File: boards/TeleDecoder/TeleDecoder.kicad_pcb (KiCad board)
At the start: 2 copper layers, 39 x 49.5 mm, 62 parts, among them J1 USB_C_Receptacle_USB2.0_16P, J2 Conn_Coaxial, J3 Conn_01x03, SW1 SW_Push, SW2 SW_Push, U1 ESP32-S3-MINI-1U, U2 TPS746-Q1, U3 CC1120, U4 ECMF02-2AMX6, Y1 STDCZS3-40M

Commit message: routing
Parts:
- moved C15 65.9 mm to (87.8, 59.8)
- moved C14 65.8 mm to (87.8, 56.8)
- moved C13 62.6 mm to (81.5, 62.0), turned to -90 degrees
- moved C20 61.4 mm to (83.0, 62.0), turned to -90 degrees
- moved C19 60.0 mm to (80.0, 62.0), turned to -90 degrees
- moved C18 55.6 mm to (75.8, 58.0), turned to 180 degrees
- moved C17 55.3 mm to (75.8, 55.0), turned to 180 degrees
- moved C16 54.2 mm to (78.0, 52.2), turned to 180 degrees
- moved R2 53.3 mm to (87.8, 58.2)
- moved C23 50.7 mm to (75.8, 59.5), turned to 180 degrees
- moved C22 50.5 mm to (75.8, 56.5), turned to 180 degrees
- moved L5 28.0 mm to (84.2, 52.2), turned to 0 degrees
- moved Y1 23.7 mm to (76.2, 61.5), turned to 180 degrees
- moved C4 22.5 mm to (78.2, 49.2)
- moved C21 21.0 mm to (78.2, 50.8)
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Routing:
- net +3V3: track 0.00 -> 20.4 mm, vias 0 -> 5
- net Net-(U3-XOSC_Q2): track 0.00 -> 7.15 mm
- net /TRX_SW: track 0.00 -> 6.91 mm
- net /LNA_N: track 0.00 -> 6.61 mm
- net Net-(U3-LPF0): track 0.00 -> 5.72 mm
- net /LNA_P: track 0.00 -> 5.48 mm
- net Net-(U3-DCPL_VCO): track 0.00 -> 4.87 mm
- net Net-(U3-LPF1): track 0.00 -> 4.52 mm
- net Net-(U3-RBIAS): track 0.00 -> 3.95 mm
- net Net-(U3-XOSC_Q1): track 0.00 -> 3.93 mm
- net Net-(U3-DCPL_XOSC): track 0.00 -> 3.63 mm
- net Net-(C3-Pad2): track 0.00 -> 3.00 mm
- net Net-(U3-DCPL_PFD_CHP): track 0.00 -> 2.48 mm
- net Net-(U3-DCPL): track 0.00 -> 1.94 mm
- net (no net): vias 0 -> 1
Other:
- copper layers 2 -> 4

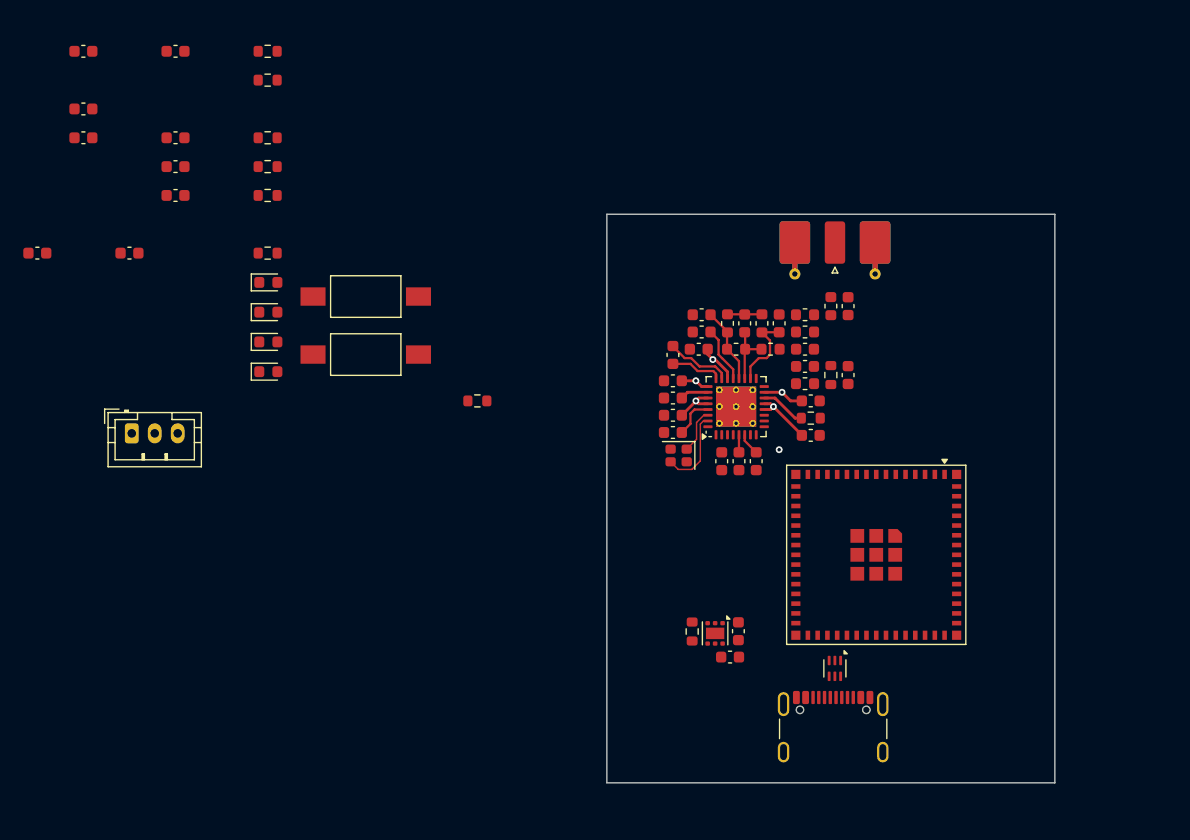
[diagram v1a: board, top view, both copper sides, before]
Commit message: Routing and minor schematic fixes
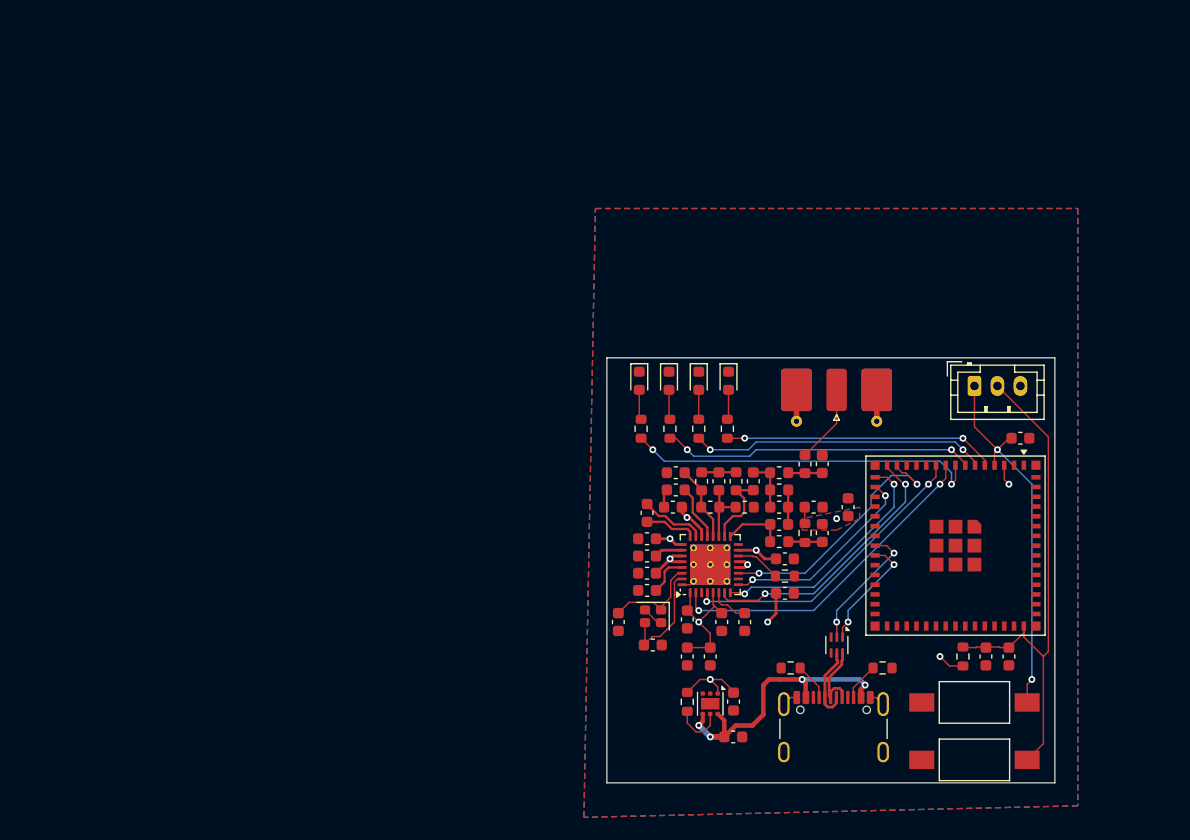
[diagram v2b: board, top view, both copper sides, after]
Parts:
- removed J1: USB_C_Receptacle_USB2.0_16P, Connector_USB:USB_C_Receptacle_GCT_USB4105-xx-A_16P_TopMnt_Horizontal
- added J101: USB4105-GF-A, Connector_USB:USB_C_Receptacle_GCT_USB4105-xx-A_16P_TopMnt_Horizontal, F.Cu at (89.7, 86.2)
- moved C28 85.5 mm to (105.0, 79.0), turned to -90 degrees
- moved C30 81.2 mm to (103.0, 79.0), turned to -90 degrees
- moved C29 77.3 mm to (106.0, 60.0)
- moved C9 74.9 mm to (88.0, 66.0)
- moved R4 74.1 mm to (94.0, 80.0)
- moved C8 74.0 mm to (91.0, 66.0), turned to 90 degrees
- moved J3 73.5 mm to (102.0, 55.5)
- moved R3 70.4 mm to (86.0, 80.0), turned to 180 degrees
- moved R10 70.0 mm to (101.0, 79.0), turned to -90 degrees
- moved C25 69.0 mm to (77.0, 79.0), turned to -90 degrees
- moved C11 68.1 mm to (74.0, 78.0)
- moved SW1 66.6 mm to (102.0, 88.0)
- moved C12 62.8 mm to (71.0, 76.0), turned to -90 degrees
- moved C24 61.6 mm to (79.0, 79.0), turned to -90 degrees
- moved SW2 61.0 mm to (102.0, 83.0)
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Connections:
- U4 pad 5: Net-(U4-D-_out) -> /D-
- U4 pad 6: Net-(U4-D+_out) -> /D+
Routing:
- net /RESET: track 0.00 -> 45.0 mm
- net /BOOT: track 0.00 -> 32.9 mm, vias 0 -> 2
- net /LED_ORANGE: track 0.00 -> 31.1 mm, vias 0 -> 2
- net /RESET_N: track 0.00 -> 29.1 mm, vias 0 -> 2
- net /LED_GREEN: track 0.00 -> 27.2 mm, vias 0 -> 2
- net /RADIO_INT: track 0.00 -> 26.2 mm, vias 0 -> 2
- net /LED_BLUE: track 0.00 -> 25.8 mm, vias 0 -> 2
- net +5V: track 0.00 -> 25.2 mm, vias 0 -> 4
- net /MOSI0: track 0.00 -> 23.7 mm, vias 0 -> 2
- net /LED_RED: track 0.00 -> 23.6 mm, vias 0 -> 2
- net /CS_RADIO: track 0.00 -> 22.5 mm, vias 0 -> 2
- net +3V3: track 20.4 -> 42.1 mm, vias 5 -> 11
- net /SCLK0: track 0.00 -> 21.3 mm, vias 0 -> 2
- net /MISO0: track 0.00 -> 17.7 mm, vias 0 -> 2
- net /USB_D-: track 0.00 -> 11.6 mm, vias 0 -> 2
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- added copper zone on F.Cu, net +3V3
- added copper zone on In2.Cu, net +3V3
- added copper zone on B.Cu, net GND
- added copper zone on F.Cu, net GND
- added copper zone on In1.Cu, net GND
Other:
- board size 39 x 49.5 mm -> 39 x 37 mm

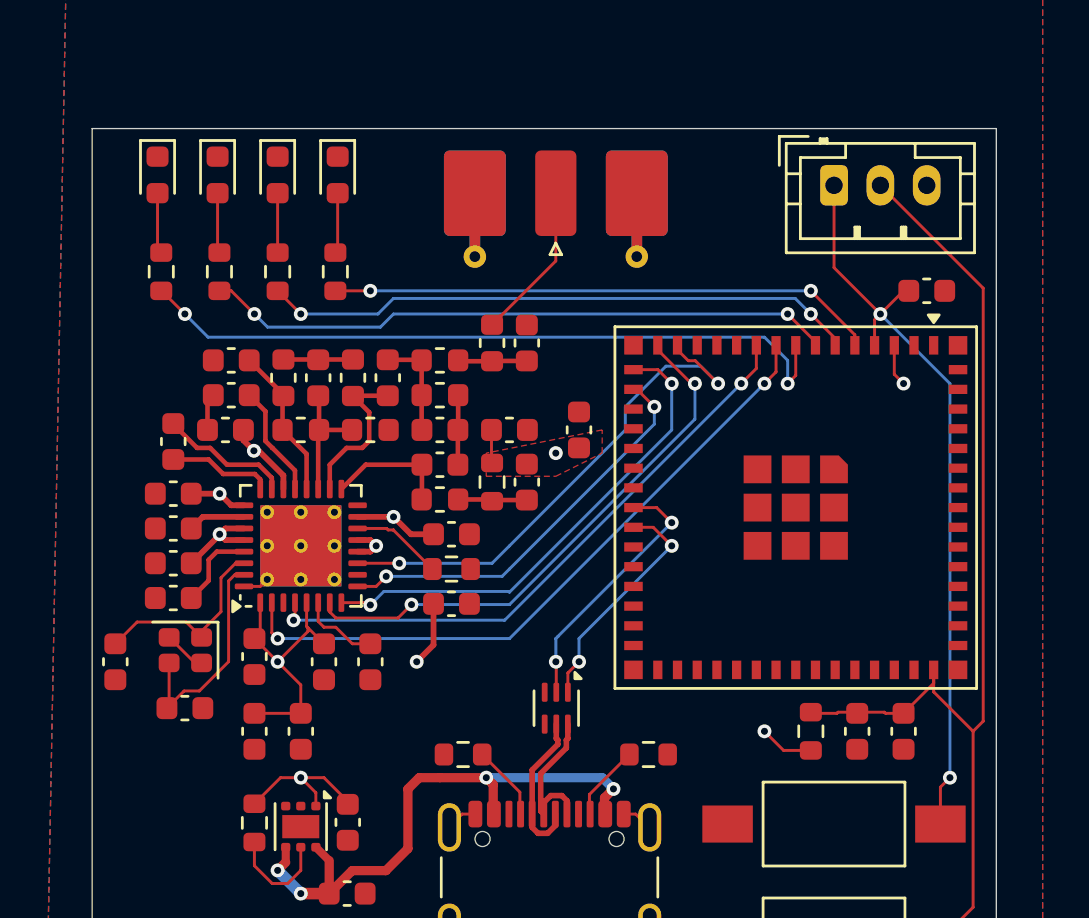
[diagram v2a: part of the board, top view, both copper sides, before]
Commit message: change gpio pins
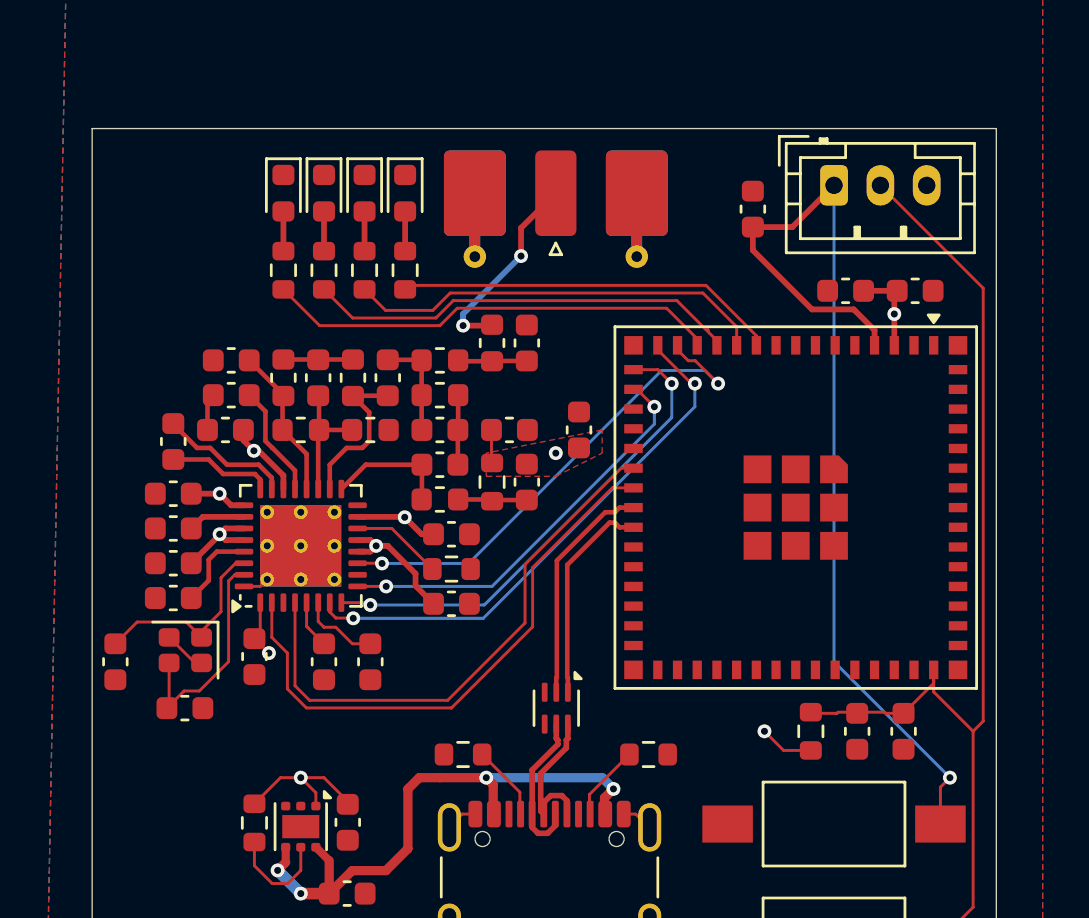
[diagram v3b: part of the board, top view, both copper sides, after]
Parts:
- moved C25 34.3 mm to (105.5, 60.0), turned to 0 degrees
- moved C24 30.2 mm to (102.5, 60.0), turned to 180 degrees
- moved D4 8.96 mm to (81.8, 55.8)
- moved R8 8.77 mm to (81.8, 59.1)
- moved C29 8.29 mm to (98.5, 56.5), turned to 90 degrees
- moved D3 4.66 mm to (80.0, 55.8)
- moved R7 4.51 mm to (80.0, 59.1)
- moved D1 3.01 mm to (83.5, 55.8)
- moved R5 3.01 mm to (83.5, 59.1)
- moved D2 0.83 mm to (78.2, 55.8)
- moved R6 0.26 mm to (78.2, 59.1)
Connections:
- U1 pad 10: /RADIO_INT -> /LED_RED
- U1 pad 11: unconnected-(U1-IO7-Pad11) -> /LED_ORANGE
- U1 pad 12: unconnected-(U1-IO8-Pad12) -> /LED_GREEN
- U1 pad 13: unconnected-(U1-IO9-Pad13) -> /LED_BLUE
- U1 pad 21: unconnected-(U1-IO17-Pad21) -> /RADIO_INT
- U1 pad 22: unconnected-(U1-IO18-Pad22) -> /RESET_N
- U1 pad 5: /LED_RED -> unconnected-(U1-IO1-Pad5)
- U1 pad 6: /LED_BLUE -> unconnected-(U1-IO2-Pad6)
- U1 pad 7: /LED_GREEN -> unconnected-(U1-IO3-Pad7)
- U1 pad 8: /LED_ORANGE -> unconnected-(U1-IO4-Pad8)
- U1 pad 9: /RESET_N -> unconnected-(U1-IO5-Pad9)
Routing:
- net /LED_ORANGE: track 31.1 -> 18.1 mm, vias 2 -> 0
- net /BOOT: track 32.9 -> 42.4 mm, vias 2 -> 1
- net /LED_GREEN: track 27.2 -> 18.7 mm, vias 2 -> 0
- net /LED_RED: track 23.6 -> 16.5 mm, vias 2 -> 0
- net /LED_BLUE: track 25.8 -> 19.6 mm, vias 2 -> 0
- net /RESET_N: track 29.1 -> 24.7 mm, vias 2 -> 0
- net +3V3: track 42.1 -> 38.0 mm, vias 11 -> 10
- net /RADIO_INT: track 26.2 -> 24.1 mm, vias 2 -> 0
- net /USB_D-: track 11.6 -> 9.94 mm, vias 2 -> 0
- net Net-(J2-In): track 7.32 -> 8.63 mm, vias 0 -> 2
- net /USB_D+: track 10.2 -> 9.20 mm, vias 2 -> 0
- net Net-(D4-A): track 2.63 -> 1.71 mm
- net Net-(D1-A): track 2.60 -> 1.71 mm
- net Net-(D3-A): track 2.60 -> 1.71 mm
- net Net-(D2-A): track 2.56 -> 1.71 mm
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
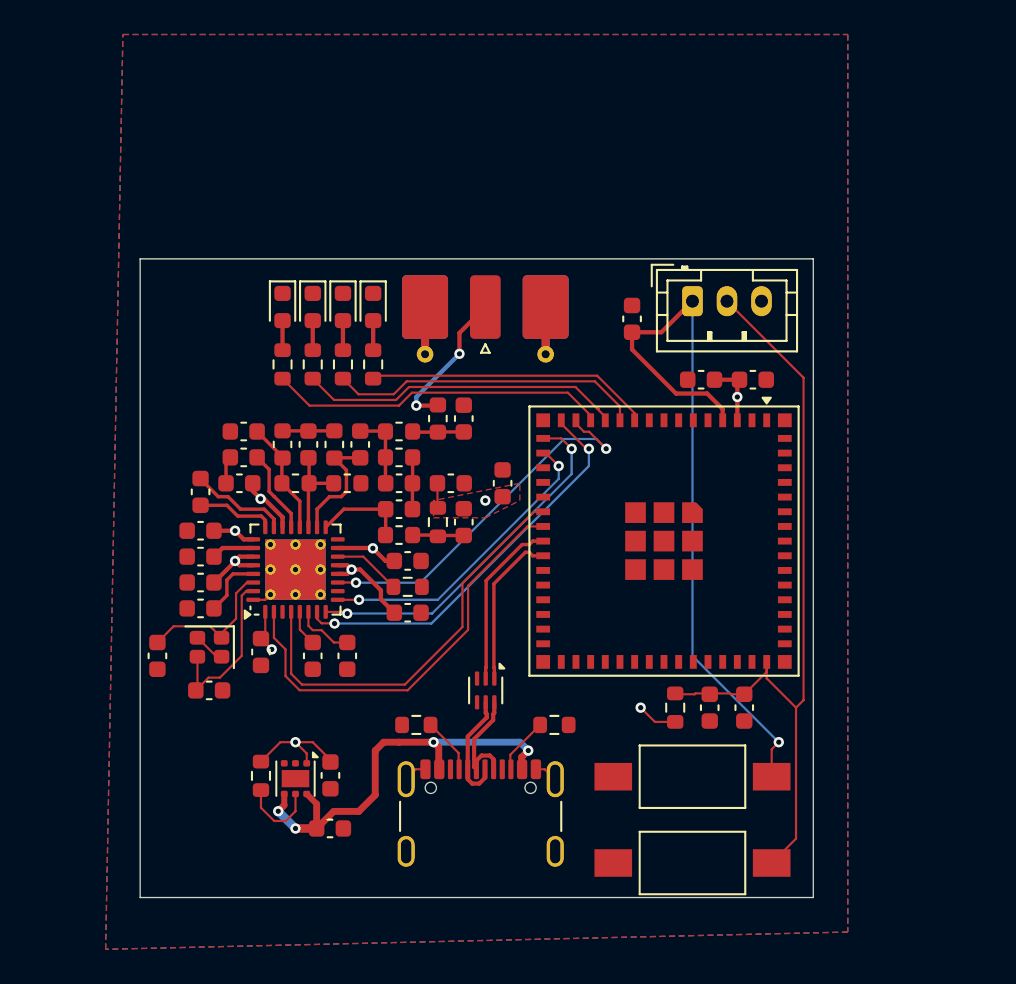
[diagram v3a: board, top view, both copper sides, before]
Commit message: Mounting holes, rerouting
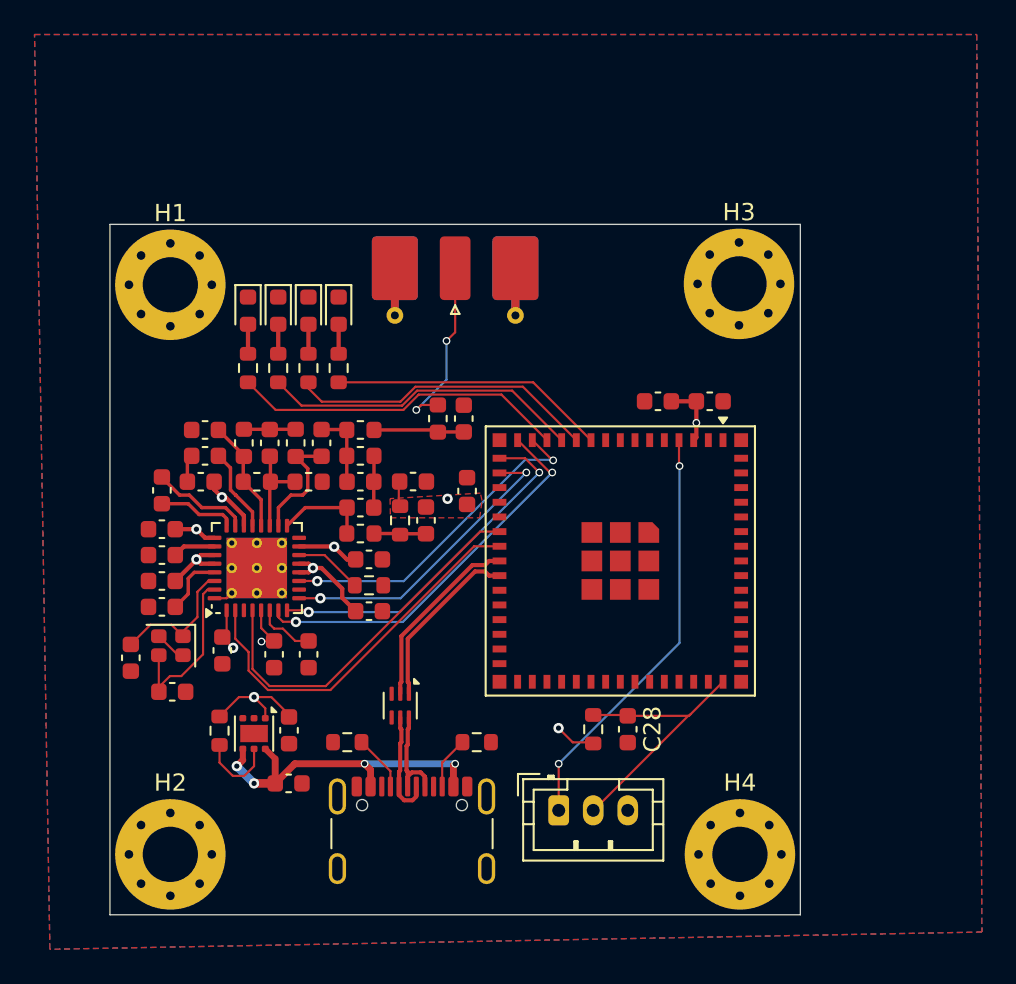
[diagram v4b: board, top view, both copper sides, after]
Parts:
- removed C29, C30: 100nF, Capacitor_SMD:C_0603_1608Metric
- removed SW1, SW2: SW_Push, Button_Switch_SMD:SW_SPST_FSMSM
- added H1: MountingHole, MountingHole:MountingHole_3.2mm_M3_Pad_Via, F.Cu at (71.8, 54.5)
- added H2: MountingHole, MountingHole:MountingHole_3.2mm_M3_Pad_Via, F.Cu at (71.8, 87.5)
- added H3: MountingHole, MountingHole:MountingHole_3.2mm_M3_Pad_Via, F.Cu at (104.7, 54.4)
- added H4: MountingHole, MountingHole:MountingHole_3.2mm_M3_Pad_Via, F.Cu at (104.8, 87.5)
- moved J3 30.5 mm to (94.2, 85.0)
- moved C28 6.86 mm to (98.2, 80.2)
- moved U4 5.03 mm to (85.1, 78.9)
- moved R10 4.91 mm to (96.2, 80.2)
- moved R4 4.61 mm to (89.5, 81.0)
- moved R3 4.12 mm to (82.0, 81.0)
- moved J101 4.10 mm to (85.8, 87.2)
- moved C26 3.55 mm to (78.6, 83.4)
- moved C27 3.55 mm to (78.6, 80.3)
- moved R9 3.55 mm to (74.6, 80.3)
- moved U2 3.55 mm to (76.6, 80.5)
- moved J2 2.85 mm to (88.2, 53.3)
- moved C24 2.80 mm to (100.0, 61.2)
- moved C25 2.80 mm to (103.0, 61.2)
- moved U1 2.78 mm to (97.8, 70.5)
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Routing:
- net /RESET: track 45.0 -> 16.1 mm
- net /BOOT: track 42.4 -> 24.4 mm, vias 1 -> 2
- net +5V: track 25.2 -> 20.0 mm
- net GND: track 7.74 -> 5.02 mm
- net /CS_RADIO: track 21.8 -> 19.3 mm
- net /RESET_N: track 24.7 -> 22.3 mm
- net Net-(C1-Pad1): track 2.98 -> 5.30 mm
- net /RADIO_INT: track 24.1 -> 21.8 mm
- net Net-(J2-In): track 8.63 -> 10.5 mm
- net /USB_D+: track 9.20 -> 10.2 mm
- net /USB_D-: track 9.94 -> 10.9 mm
- net /MOSI0: track 23.4 -> 22.7 mm
- net +3V3: track 38.0 -> 38.6 mm, vias 10 -> 11
- net Net-(U3-XOSC_Q1): track 8.31 -> 7.70 mm
- net /LED_RED: track 16.5 -> 16.0 mm
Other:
- board size 39 x 37 mm -> 40 x 40 mm

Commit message: Debug pins, silkscreen
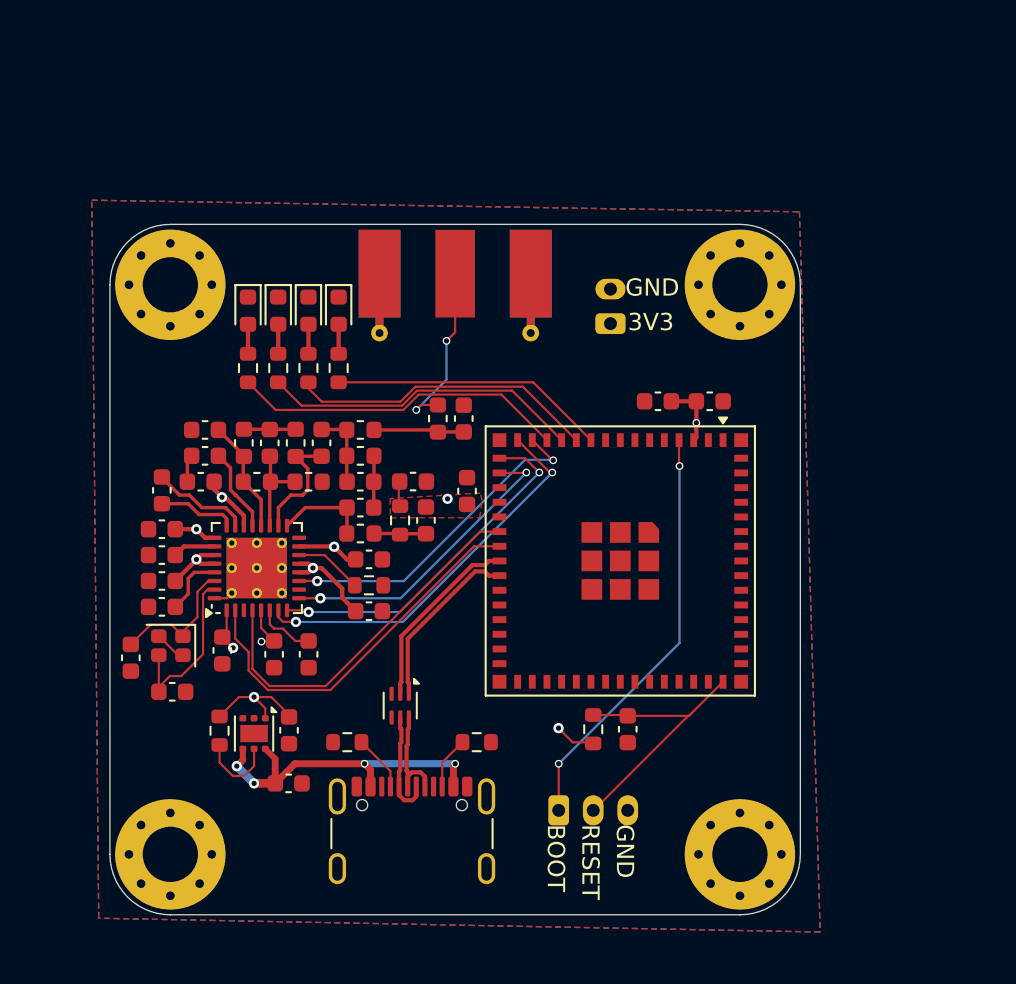
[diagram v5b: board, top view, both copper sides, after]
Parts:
- added J1: Conn_01x02, Connector_JST:JST_PH_B2B-PH-K_1x02_P2.00mm_Vertical, F.Cu at (97.2, 56.8)
- J2: footprint Connector_Coaxial:SMA_Molex_73251-2120_EdgeMount_Horizontal -> Connector_Coax:SMA_Molex_732511153_EdgeMount_Horizontal
- moved J2 2.29 mm to (88.2, 55.6), turned to -90 degrees
- moved H3 0.07 mm to (104.8, 54.5)
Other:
- outline, holes or cut-outs redrawn
- board text added: "3V3"
- board text added: "BOOT"
- board text added: "GND"
- board text added: "RESET"
